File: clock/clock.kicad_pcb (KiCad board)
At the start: 2 copper layers, 100 x 50 mm, 88 parts, among them J1 USB_OTG-conn1, SW1 SW_SPST, SW2 SW_SPST, SW3 SW_SPST, SW4 SW_SPST, SW5 SW_SPST, U1 iv12, U10 PCA9685PW, U11 ATmega32U4-AU, U12 DS3231M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

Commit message: Rev 4 PCB
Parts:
- removed C5, C9: .1u, Capacitor_SMD:C_0603_1608Metric_Pad1.05x0.95mm_HandSolder
- removed C7, C8: 22p, Capacitor_SMD:C_0603_1608Metric_Pad1.05x0.95mm_HandSolder
- removed R41, R42: 22, Resistor_SMD:R_0603_1608Metric_Pad1.05x0.95mm_HandSolder
- removed TP1, TP2, TP3, TP4, TP5: TestPoint, TestPoint:TestPoint_Plated_Hole_D2.0mm
- added J2: USB, Connector_USB:USB_Micro-B_Molex-105133-0001, B.Cu at (127.0, 149.0)
- added J3: TP, Connector_PinHeader_2.54mm:PinHeader_1x05_P2.54mm_Vertical, B.Cu at (120.1, 149.0)
- J1: value USB_OTG-conn1 -> FTDI; footprint Connector_USB:USB_Micro-B_Molex-105133-0001 -> Connector_PinHeader_2.54mm:PinHeader_1x06_P2.54mm_Vertical
- L1: value L_Small -> 22 uH
- U11: value ATmega32U4-AU -> ATmega328P-AU; footprint Package_DFN_QFN:QFN-44-1EP_7x7mm_P0.5mm_EP5.15x5.15mm -> Package_QFP:TQFP-32_7x7mm_P0.8mm
- Y1: value 16Mhz -> 16MHz; footprint Crystal:Crystal_SMD_5032-4Pin_5.0x3.2mm -> Crystal:Resonator_SMD_muRata_CSTxExxV-3Pin_3.0x1.1mm_HandSoldering
- moved J1 48.7 mm to (108.5, 104.0), turned to 270 degrees
- moved C6 27.8 mm to (105.0, 114.3), turned to 90 degrees
- moved Y1 14.6 mm to (130.0, 104.7)
- moved C4 10.6 mm to (129.0, 119.6), turned to 270 degrees
- moved R43 3.50 mm to (130.5, 119.6)
- moved C3 2.90 mm to (126.6, 104.7)
- moved R39 1.55 mm to (122.2, 119.0)
- moved R40 1.45 mm to (120.7, 119.0)
- moved U11 1.00 mm to (127.0, 112.0), turned to 270 degrees
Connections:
- J1 pad 1: +5V -> GND
- J1 pad 2: Net-(J1-Pad2) -> CTS
- J1 pad 4: GND -> RX
- J1 pad 5: GND -> TX
- J1 pad 6: GND -> RST
- U11 pad 10: MODE -> Net-(U11-Pad10)
- U11 pad 11: OTHER -> Net-(U11-Pad11)
- U11 pad 12: Net-(U11-Pad12) -> UP
- U11 pad 13: RST -> DOWN
- U11 pad 14: +5V -> MODE
- U11 pad 15: GND -> OTHER
- U11 pad 16: Net-(C8-Pad1) -> Net-(U11-Pad16)
- U11 pad 17: Net-(C7-Pad1) -> Net-(U11-Pad17)
- U11 pad 18: SCL -> +5V
- U11 pad 19: SDA -> Net-(U11-Pad19)
- U11 pad 2: +5V -> Net-(U11-Pad2)
- U11 pad 21: Net-(U11-Pad21) -> GND
- U11 pad 23: GND -> Net-(U11-Pad23)
- U11 pad 24: +5V -> Net-(U11-Pad24)
- U11 pad 27: Net-(U11-Pad27) -> SDA
- U11 pad 28: Net-(U11-Pad28) -> SCL
- U11 pad 29: Net-(U11-Pad29) -> RST
- U11 pad 3: Net-(R42-Pad1) -> GND
- U11 pad 30: Net-(U11-Pad30) -> RX
- U11 pad 31: Net-(U11-Pad31) -> TX
- U11 pad 4: Net-(R41-Pad1) -> +5V
- U11 pad 6: Net-(U11-Pad6) -> +5V
- U11 pad 8: UP -> Net-(U11-Pad8)
- U11 pad 9: DOWN -> Net-(U11-Pad9)
- Y1 pad 1: Net-(C7-Pad1) -> Net-(U11-Pad7)
- Y1 pad 2: Net-(Y1-Pad2) -> Net-(U11-Pad8)
- Y1 pad 3: Net-(C8-Pad1) -> GND
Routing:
- net Net-(R42-Pad1): track 64.3 -> 0.00 mm, vias 2 -> 0
- net Net-(R41-Pad1): track 62.6 -> 0.00 mm, vias 2 -> 0
- net RST: track 21.6 -> 49.2 mm, vias 0 -> 3
- net +5V: track 301.5 -> 288.5 mm
- net Net-(J1-Pad3): track 11.4 -> 0.00 mm
- net Net-(J1-Pad2): track 10.6 -> 0.00 mm
- net RX: track 0.00 -> 10.1 mm
- net Net-(C8-Pad1): track 8.70 -> 0.00 mm
- net TX: track 0.00 -> 8.25 mm
- net Net-(C7-Pad1): track 6.70 -> 0.00 mm
- net SDA: track 122.9 -> 119.2 mm, vias 2 -> 3
- net SCL: track 123.6 -> 120.4 mm
- net Net-(U11-Pad8): track 0.00 -> 3.13 mm
- net Net-(U11-Pad7): track 0.00 -> 3.13 mm
- net MODE: track 48.1 -> 49.5 mm
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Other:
- board text added: "24v"
- board text added: "5v"
- board text added: "IV-12 Clock https://github.com/Wiles/iv-12 Rev. 4"
- board text added: "SCL"
- board text added: "SDA"
- board text removed: "IV-12 Clock https://github.com/Wiles/iv-12 Rev. 3"

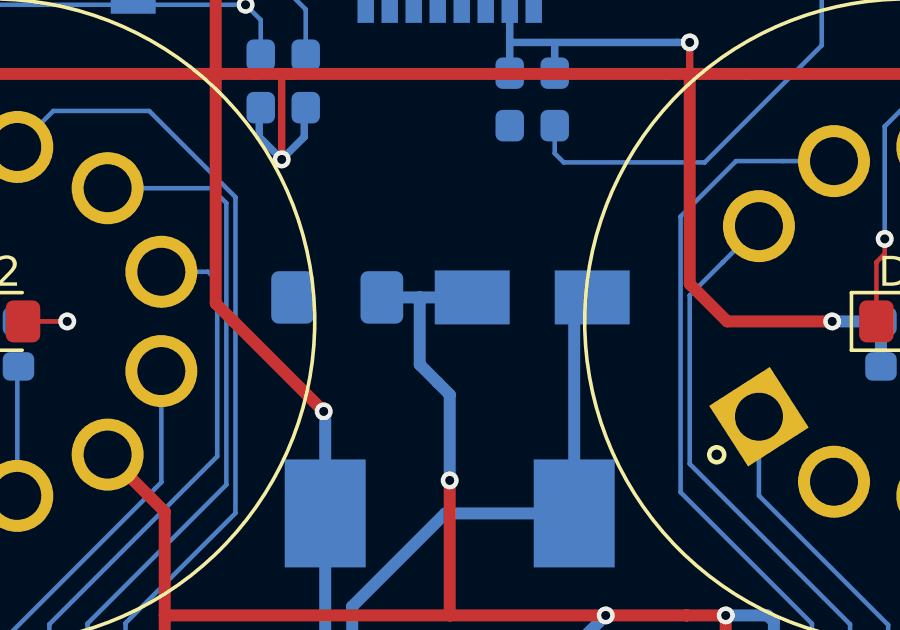
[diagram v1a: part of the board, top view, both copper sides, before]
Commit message: Readded OSHW logo
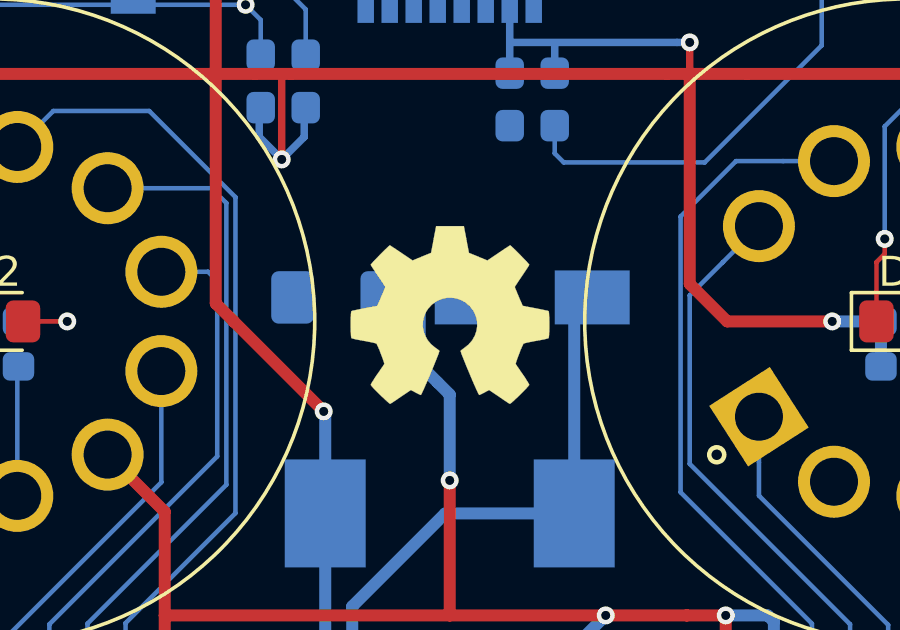
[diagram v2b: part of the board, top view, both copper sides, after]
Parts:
- added REF**: OSHW-Symbol_6.7x6mm_SilkScreen, Symbol:OSHW-Symbol_6.7x6mm_SilkScreen, F.Cu at (127.0, 126.8)

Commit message: Layout cleanup
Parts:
- moved R40 3.60 mm to (124.1, 120.1), turned to 180 degrees
- moved R39 1.97 mm to (124.1, 118.6), turned to 0 degrees
- moved C4 1.33 mm to (129.9, 118.6), turned to 0 degrees
- moved R43 0.80 mm to (129.9, 120.1), turned to 180 degrees
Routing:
- net SCL: track 120.4 -> 126.4 mm
- net +5V: track 288.5 -> 285.4 mm, vias 13 -> 12
- net Net-(D5-Pad2): track 23.0 -> 20.6 mm
- net SDA: track 119.2 -> 121.4 mm
- net RST: track 49.2 -> 47.3 mm
- net +24V: track 264.0 -> 262.7 mm
- net Net-(R6-Pad2): track 25.2 -> 24.1 mm
- net Net-(R10-Pad2): track 20.9 -> 20.0 mm
- net Net-(R2-Pad2): track 29.9 -> 29.1 mm
- net Net-(BT1-Pad1): track 27.1 -> 26.4 mm

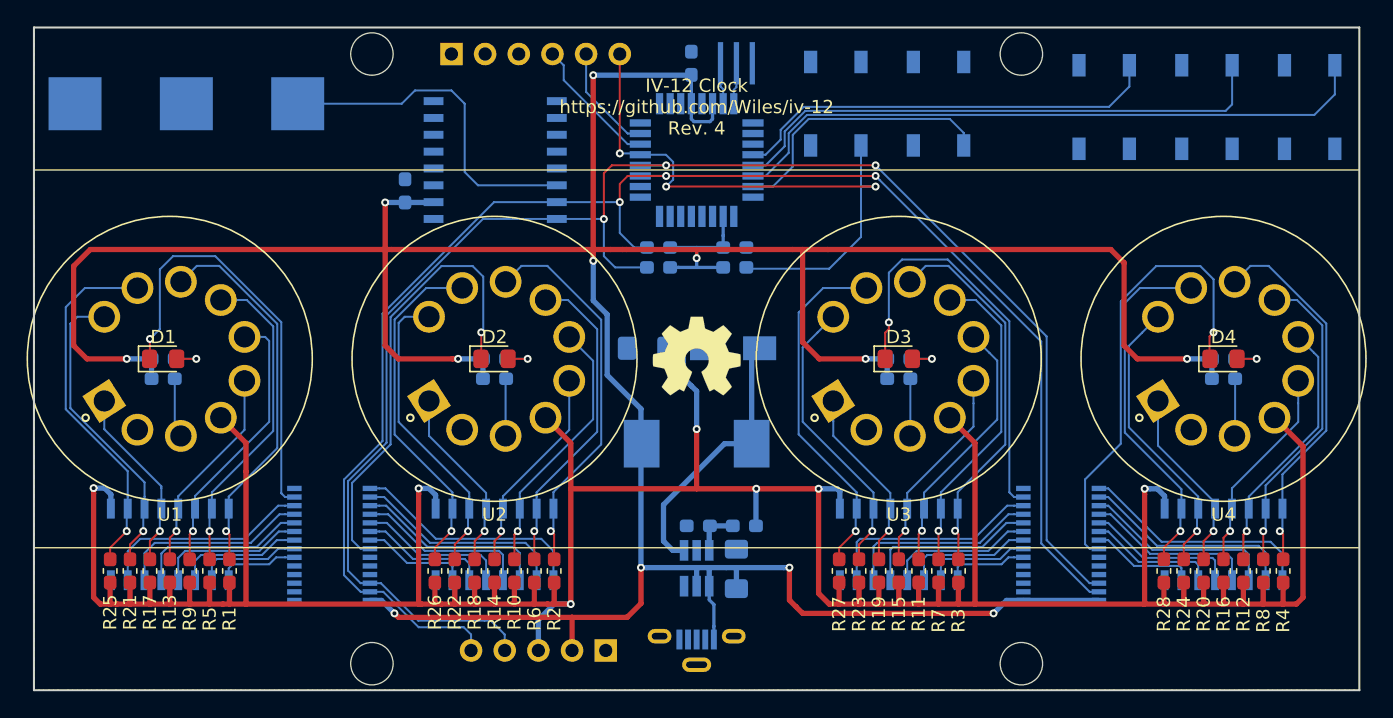
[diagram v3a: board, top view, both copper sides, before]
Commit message: Hooked up SQW from RTC to MCU
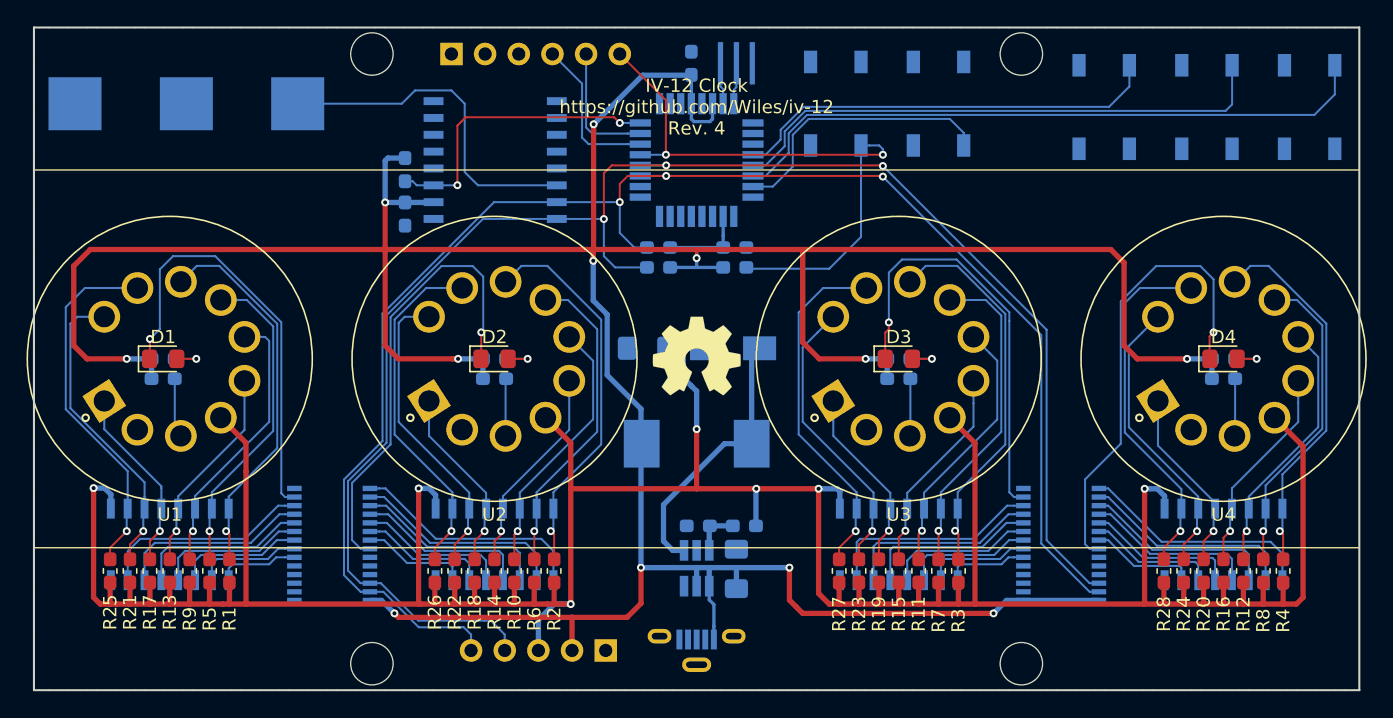
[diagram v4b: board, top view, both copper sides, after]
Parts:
- added R41: 10k, Resistor_SMD:R_0603_1608Metric_Pad1.05x0.95mm_HandSolder, B.Cu at (105.0, 112.7)
- moved C6 1.75 mm to (105.0, 116.1), turned to 270 degrees
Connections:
- U11 pad 32: Net-(U11-Pad32) -> SQW
- U12 pad 3: Net-(U12-Pad3) -> SQW
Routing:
- net SQW: track 0.00 -> 22.8 mm, vias 0 -> 2
- net +5V: track 285.4 -> 288.0 mm
- net RX: track 10.1 -> 11.8 mm
- net TX: track 8.25 -> 9.82 mm
- net RST: track 47.3 -> 46.1 mm, vias 3 -> 2

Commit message: More cleanup
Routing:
- net +5V: track 288.0 -> 288.8 mm
- net SDA: track 121.7 -> 122.3 mm
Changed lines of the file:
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@@
     (thickness 1.6)
     (drawings 11)
-    (tracks 901)
+    (tracks 902)
     (zones 0)
     (modules 81)
@@
   (segment (start 134 142.75) (end 134 145.199996) (width 0.4) (layer F.Cu) (net 31))
   (segment (start 135.000004 146.2) (end 134.5 145.699996) (width 0.4) (layer F.Cu) (net 31))
-  (segment (start 126.574999 105.6) (end 122.928012 105.6) (width 0.4) (layer B.Cu) (net 31))
   (segment (start 119.22801 109.724266) (end 119.22801 109.300002) (width 0.4) (layer F.Cu) (net 31))
-  (segment (start 122.928012 105.6) (end 119.528009 109.000003) (width 0.4) (layer B.Cu) (net 31))
-  (segment (start 119.528009 109.000003) (end 119.22801 109.300002) (width 0.4) (layer B.Cu) (net 31))
   (segment (start 119.22801 118.72199) (end 119.22801 109.724266) (width 0.4) (layer F.Cu) (net 31))
   (segment (start 119.2 118.75) (end 119.22801 118.72199) (width 0.4) (layer F.Cu) (net 31))
@@
   (segment (start 103.5 115.2) (end 103.5 112.05) (width 0.4) (layer B.Cu) (net 31))
   (segment (start 103.5 112.05) (end 103.7 111.85) (width 0.4) (layer B.Cu) (net 31))
+  (segment (start 119.25 109.278012) (end 119.22801 109.300002) (width 0.4) (layer B.Cu) (net 31))
+  (segment (start 119.25 107.8) (end 119.25 109.278012) (width 0.4) (layer B.Cu) (net 31))
+  (segment (start 126.574999 105.6) (end 121.45 105.6) (width 0.4) (layer B.Cu) (net 31))
+  (segment (start 121.45 105.6) (end 119.25 107.8) (width 0.4) (layer B.Cu) (net 31))
   (segment (start 143.125 132.776301) (end 143.0861 132.815201) (width 0.152) (layer B.Cu) (net 32) (status 30))
   (segment (start 143.125 128.5) (end 143.125 132.776301) (width 0.152) (layer B.Cu) (net 32) (status 30))
@@
   (segment (start 109.1 147.25) (end 109.3 147.25) (width 0.152) (layer B.Cu) (net 72))
   (segment (start 124.7 113.2) (end 122.75 113.2) (width 0.152) (layer B.Cu) (net 72))
-  (segment (start 116.45 115.175) (end 121.19999 115.175) (width 0.152) (layer B.Cu) (net 72))
-  (segment (start 122.29999 118.6) (end 121.19999 117.5) (width 0.152) (layer B.Cu) (net 72))
-  (segment (start 123.25 118.6) (end 122.29999 118.6) (width 0.152) (layer B.Cu) (net 72))
-  (segment (start 121.19999 115.175) (end 121.19999 117.5) (width 0.152) (layer B.Cu) (net 72))
-  (via (at 121.19999 115.175) (size 0.6) (drill 0.3) (layers F.Cu B.Cu) (net 72))
   (via (at 124.7 113.2) (size 0.6) (drill 0.3) (layers F.Cu B.Cu) (net 72))
-  (segment (start 121.8 113.2) (end 124.7 113.2) (width 0.152) (layer F.Cu) (net 72))
-  (segment (start 121.19999 115.175) (end 121.19999 113.80001) (width 0.152) (layer F.Cu) (net 72))
-  (segment (start 121.19999 113.80001) (end 121.8 113.2) (width 0.152) (layer F.Cu) (net 72))
   (via (at 141.05 113.25) (size 0.6) (drill 0.3) (layers F.Cu B.Cu) (net 72))
   (segment (start 157.35 144.575) (end 156.648 144.575) (width 0.152) (layer B.Cu) (net 72))
@@
   (segment (start 156.648 144.575) (end 153 140.927) (width 0.152) (layer B.Cu) (net 72))
   (segment (start 124.7 113.2) (end 141 113.2) (width 0.152) (layer F.Cu) (net 72))
+  (segment (start 124.7 113.2) (end 121.2 113.2) (width 0.152) (layer F.Cu) (net 72))
+  (segment (start 121.2 113.624264) (end 121.2 113.2) (width 0.152) (layer B.Cu) (net 72))
+  (segment (start 121.2 116.55) (end 121.2 113.624264) (width 0.152) (layer B.Cu) (net 72))
+  (segment (start 123.25 118.6) (end 121.2 116.55) (width 0.152) (layer B.Cu) (net 72))
+  (via (at 121.2 113.2) (size 0.6) (drill 0.3) (layers F.Cu B.Cu) (net 72))
+  (segment (start 120.05 113.2) (end 121.2 113.2) (width 0.152) (layer B.Cu) (net 72))
+  (segment (start 116.45 115.175) (end 118.075 115.175) (width 0.152) (layer B.Cu) (net 72))
+  (segment (start 118.075 115.175) (end 120.05 113.2) (width 0.152) (layer B.Cu) (net 72))
   (segment (start 110.875066 116.445) (end 103.604011 123.716055) (width 0.152) (layer B.Cu) (net 73))
   (segment (start 116.45 116.445) (end 110.875066 116.445) (width 0.152) (layer B.Cu) (net 73) (status 10))
@@
   (segment (start 131.15 126.8) (end 131.75 126.2) (width 0.4) (layer B.Cu) (net 81) (status 30))
   (segment (start 131.15 133.4) (end 131.15 126.8) (width 0.4) (layer B.Cu) (net 81) (status 30))
-  (segment (start 129.1 133.4) (end 131.15 133.4) (width 0.4) (layer B.Cu) (net 81))
-  (segment (start 124.5 138) (end 129.1 133.4) (width 0.4) (layer B.Cu) (net 81))
-  (segment (start 124.5 140.75) (end 124.5 138) (width 0.4) (layer B.Cu) (net 81))
+  (segment (start 129.2 133.4) (end 131.15 133.4) (width 0.4) (layer B.Cu) (net 81))
+  (segment (start 124.9 137.7) (end 129.2 133.4) (width 0.4) (layer B.Cu) (net 81))
+  (segment (start 124.9 141.15) (end 124.9 137.7) (width 0.4) (layer B.Cu) (net 81))
   (segment (start 126.05 141.45) (end 125.2 141.45) (width 0.4) (layer B.Cu) (net 81))
-  (segment (start 125.2 141.45) (end 124.5 140.75) (width 0.4) (layer B.Cu) (net 81))
+  (segment (start 125.2 141.45) (end 124.9 141.15) (width 0.4) (layer B.Cu) (net 81))
   (segment (start 127.95 139.65) (end 128 139.6) (width 0.4) (layer B.Cu) (net 82) (status 30))
   (segment (start 127.95 141.45) (end 127.95 139.65) (width 0.4) (layer B.Cu) (net 82) (status 30))
@@
   (segment (start 108.95 113.9) (end 108.95 109.4) (width 0.152) (layer F.Cu) (net 107))
   (segment (start 108.95 109.4) (end 109.577999 108.772001) (width 0.152) (layer F.Cu) (net 107))
-  (segment (start 105.88 113.905) (end 107.15 113.905) (width 0.152) (layer B.Cu) (net 107))
-  (segment (start 105 113.6) (end 105.575 113.6) (width 0.152) (layer B.Cu) (net 107))
-  (segment (start 105.575 113.6) (end 105.88 113.905) (width 0.152) (layer B.Cu) (net 107))
+  (segment (start 106.105 113.905) (end 107.15 113.905) (width 0.152) (layer B.Cu) (net 107))
+  (segment (start 105 113.6) (end 105.8 113.6) (width 0.152) (layer B.Cu) (net 107))
+  (segment (start 105.8 113.6) (end 106.105 113.905) (width 0.152) (layer B.Cu) (net 107))
   (zone (net 1) (net_name GND) (layer B.Cu) (hatch edge 0.508)
     (connect_pads (clearance 0.254))
